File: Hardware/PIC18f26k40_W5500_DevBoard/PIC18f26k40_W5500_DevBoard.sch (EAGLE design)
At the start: 77 parts, among them J2 MAGJACK, J6 USB-B, T1 BT138-H, U1 W5500, U2 PIC18F2523-I/SO, Y2 CRYSTAL-GROUNDEDSMD-3.2X2.5

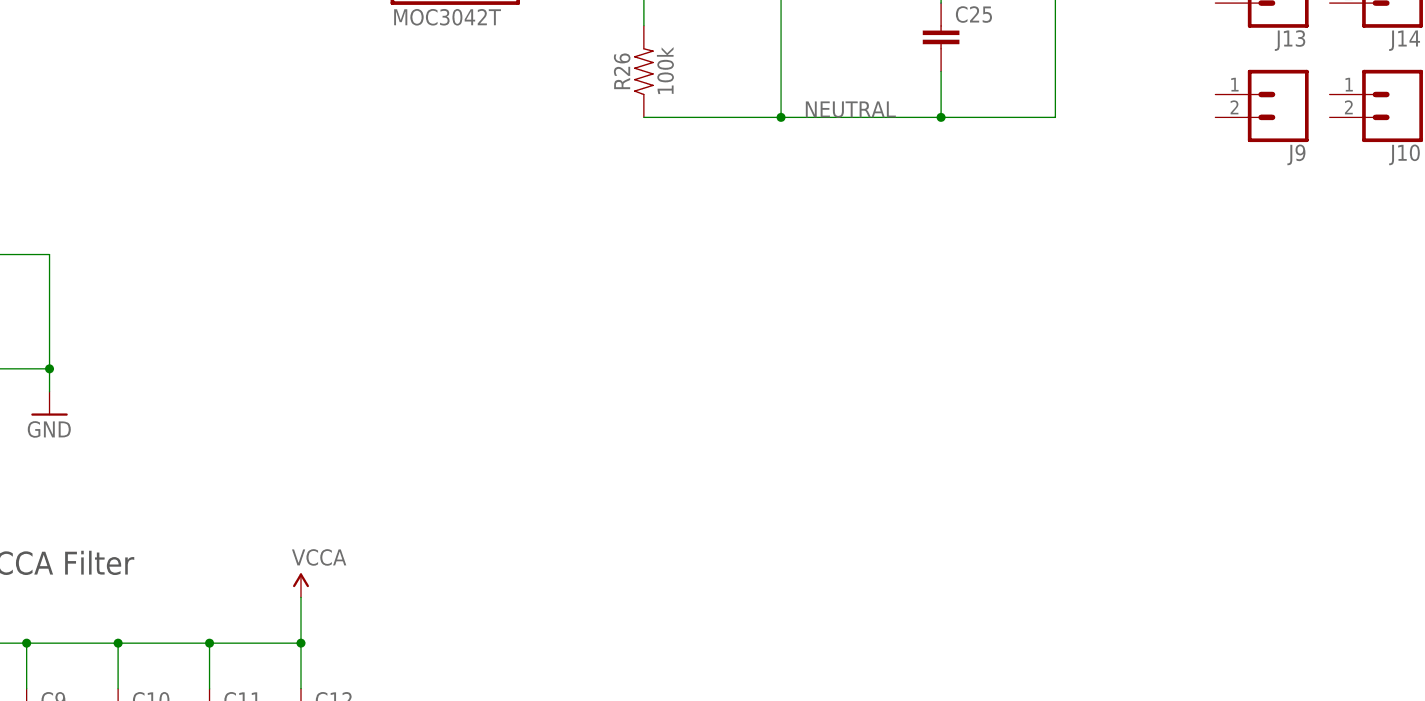
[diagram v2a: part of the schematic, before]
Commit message: #302 Added a second AC Playgorund
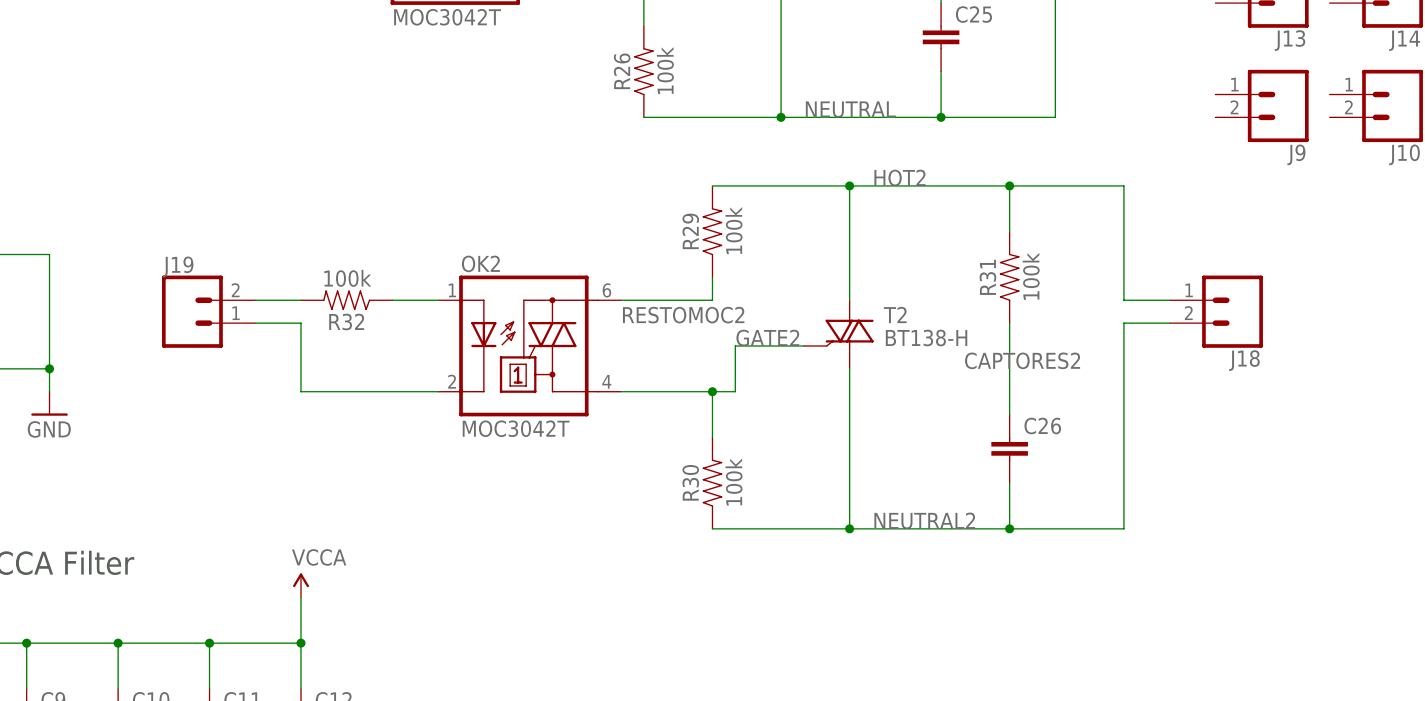
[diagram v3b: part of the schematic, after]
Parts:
- added C26: (no value), SparkFun-Capacitors:CAPPTH3
- added J18: (no value), SparkFun-Connectors:CONN_025MM
- added J19: (no value), SparkFun-Connectors:CONN_02
- added OK2: MOC3042T, optocoupler:MOC3042T
- added R29, R30, R31, R32: 100k, SparkFun-Resistors:100KOHM-HORIZ-1/4W-1%
- added T2: BT138-H, triac:BT138-H
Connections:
- new net CAPTORES2: C26.1, R31.1
- new net GATE2: OK2.A1, R30.2, T2.G
- new net HOT2: J18.1, R29.2, R31.2, T2.A2
- new net N$20: J19.2, R32.2
- new net N$21: OK2.A, R32.1
- new net N$22: J19.1, OK2.C
- new net NEUTRAL2: C26.2, J18.2, R30.1, T2.A1
- new net RESTOMOC2: OK2.A2, R29.1
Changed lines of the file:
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@@
 <part name="J16" library="SparkFun-Connectors" deviceset="CONN_02" device="5MM"/>
 <part name="J17" library="SparkFun-Connectors" deviceset="CONN_02" device="5MM"/>
+<part name="OK2" library="optocoupler" deviceset="MOC30*" device="T" technology="42"/>
+<part name="J18" library="SparkFun-Connectors" deviceset="CONN_02" device="5MM"/>
+<part name="R29" library="SparkFun-Resistors" deviceset="100KOHM" device="-HORIZ-1/4W-1%" value="100k"/>
+<part name="R30" library="SparkFun-Resistors" deviceset="100KOHM" device="-HORIZ-1/4W-1%" value="100k"/>
+<part name="T2" library="triac" deviceset="BT138" device="-H"/>
+<part name="C26" library="SparkFun-Capacitors" deviceset="CAP" device="PTH3"/>
+<part name="R31" library="SparkFun-Resistors" deviceset="100KOHM" device="-HORIZ-1/4W-1%" value="100k"/>
+<part name="R32" library="SparkFun-Resistors" deviceset="100KOHM" device="-HORIZ-1/4W-1%" value="100k"/>
+<part name="J19" library="SparkFun-Connectors" deviceset="CONN_02" device=""/>
 </parts>
 <sheets>
@@
 <instance part="J16" gate="G$1" x="477.52" y="132.08" rot="R180"/>
 <instance part="J17" gate="G$1" x="477.52" y="119.38" rot="R180"/>
+<instance part="OK2" gate="-1" x="368.3" y="78.74"/>
+<instance part="J18" gate="G$1" x="447.04" y="83.82" rot="R180"/>
+<instance part="R29" gate="G$1" x="388.62" y="91.44" rot="R90"/>
+<instance part="R30" gate="G$1" x="388.62" y="63.5" rot="R90"/>
+<instance part="T2" gate="G$1" x="403.86" y="78.74"/>
+<instance part="C26" gate="G$1" x="421.64" y="66.04"/>
+<instance part="R31" gate="G$1" x="421.64" y="86.36" rot="R90"/>
+<instance part="R32" gate="G$1" x="347.98" y="83.82" rot="R180"/>
+<instance part="J19" gate="G$1" x="330.2" y="81.28"/>
 </instances>
 <busses>
@@
 </segment>
 </net>
+<net name="N$20" class="0">
+<segment>
+<pinref part="J19" gate="G$1" pin="2"/>
+<pinref part="R32" gate="G$1" pin="2"/>
+<wire x1="337.82" y1="83.82" x2="342.9" y2="83.82" width="0.1524" layer="91"/>
+</segment>
+</net>
+<net name="N$21" class="0">
+<segment>
+<pinref part="R32" gate="G$1" pin="1"/>
+<pinref part="OK2" gate="-1" pin="A"/>
+<wire x1="353.06" y1="83.82" x2="358.14" y2="83.82" width="0.1524" layer="91"/>
+</segment>
+</net>
+<net name="N$22" class="0">
+<segment>
+<pinref part="OK2" gate="-1" pin="C"/>
+<wire x1="358.14" y1="73.66" x2="342.9" y2="73.66" width="0.1524" layer="91"/>
+<wire x1="342.9" y1="73.66" x2="342.9" y2="81.28" width="0.1524" layer="91"/>
+<pinref part="J19" gate="G$1" pin="1"/>
+<wire x1="342.9" y1="81.28" x2="337.82" y2="81.28" width="0.1524" layer="91"/>
+</segment>
+</net>
+<net name="RESTOMOC2" class="0">
+<segment>
+<pinref part="R29" gate="G$1" pin="1"/>
+<wire x1="388.62" y1="86.36" x2="388.62" y2="83.82" width="0.1524" layer="91"/>
+<pinref part="OK2" gate="-1" pin="A2"/>
+<wire x1="388.62" y1="83.82" x2="378.46" y2="83.82" width="0.1524" layer="91"/>
+<label x="378.46" y="81.28" size="1.778" layer="95"/>
+</segment>
+</net>
+<net name="GATE2" class="0">
+<segment>
+<pinref part="OK2" gate="-1" pin="A1"/>
+<wire x1="378.46" y1="73.66" x2="388.62" y2="73.66" width="0.1524" layer="91"/>
+<wire x1="388.62" y1="73.66" x2="391.16" y2="73.66" width="0.1524" layer="91"/>
+<wire x1="391.16" y1="73.66" x2="391.16" y2="78.74" width="0.1524" layer="91"/>
+<pinref part="T2" gate="G$1" pin="G"/>
+<wire x1="391.16" y1="78.74" x2="398.78" y2="78.74" width="0.1524" layer="91"/>
+<pinref part="R30" gate="G$1" pin="2"/>
+<wire x1="388.62" y1="68.58" x2="388.62" y2="73.66" width="0.1524" layer="91"/>
+<junction x="388.62" y="73.66"/>
+<label x="391.16" y="78.74" size="1.778" layer="95"/>
+</segment>
+</net>
+<net name="HOT2" class="0">
+<segment>
+<pinref part="T2" gate="G$1" pin="A2"/>
+<wire x1="403.86" y1="83.82" x2="403.86" y2="96.52" width="0.1524" layer="91"/>
+<pinref part="R29" gate="G$1" pin="2"/>
+<wire x1="403.86" y1="96.52" x2="388.62" y2="96.52" width="0.1524" layer="91"/>
+<pinref part="J18" gate="G$1" pin="1"/>
+<wire x1="439.42" y1="83.82" x2="434.34" y2="83.82" width="0.1524" layer="91"/>
+<wire x1="434.34" y1="83.82" x2="434.34" y2="96.52" width="0.1524" layer="91"/>
+<wire x1="434.34" y1="96.52" x2="421.64" y2="96.52" width="0.1524" layer="91"/>
+<junction x="403.86" y="96.52"/>
+<pinref part="R31" gate="G$1" pin="2"/>
+<wire x1="421.64" y1="96.52" x2="403.86" y2="96.52" width="0.1524" layer="91"/>
+<wire x1="421.64" y1="91.44" x2="421.64" y2="96.52" width="0.1524" layer="91"/>
+<junction x="421.64" y="96.52"/>
+<label x="406.4" y="96.52" size="1.778" layer="95"/>
+</segment>
+</net>
+<net name="CAPTORES2" class="0">
+<segment>
+<pinref part="C26" gate="G$1" pin="1"/>
+<pinref part="R31" gate="G$1" pin="1"/>
+<wire x1="421.64" y1="71.12" x2="421.64" y2="81.28" width="0.1524" layer="91"/>
+<label x="416.56" y="76.2" size="1.778" layer="95"/>
+</segment>
+</net>
+<net name="NEUTRAL2" class="0">
+<segment>
+<pinref part="J18" gate="G$1" pin="2"/>
+<wire x1="439.42" y1="81.28" x2="434.34" y2="81.28" width="0.1524" layer="91"/>
+<wire x1="434.34" y1="81.28" x2="434.34" y2="58.42" width="0.1524" layer="91"/>
+<pinref part="R30" gate="G$1" pin="1"/>
+<wire x1="434.34" y1="58.42" x2="421.64" y2="58.42" width="0.1524" layer="91"/>
+<pinref part="T2" gate="G$1" pin="A1"/>
+<wire x1="421.64" y1="58.42" x2="403.86" y2="58.42" width="0.1524" layer="91"/>
+<wire x1="403.86" y1="58.42" x2="388.62" y2="58.42" width="0.1524" layer="91"/>
+<wire x1="403.86" y1="76.2" x2="403.86" y2="58.42" width="0.1524" layer="91"/>
+<junction x="403.86" y="58.42"/>
+<pinref part="C26" gate="G$1" pin="2"/>
+<wire x1="421.64" y1="63.5" x2="421.64" y2="58.42" width="0.1524" layer="91"/>
+<junction x="421.64" y="58.42"/>
+<label x="406.4" y="58.42" size="1.778" layer="95"/>
+</segment>
+</net>
